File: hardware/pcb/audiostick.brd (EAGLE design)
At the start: 84 x 34 mm, 61 parts, among them IC1 TPS73633MBDV, IC3 PCM5102ASW, IC5 AP22804W5, IC6 TINY13V-10SSU, J1 AVRISP6TH127, J2 AUDIO_JACK_3.5MM_PTH, J3 USB-B, SW1 EVQP7, T1 BC850

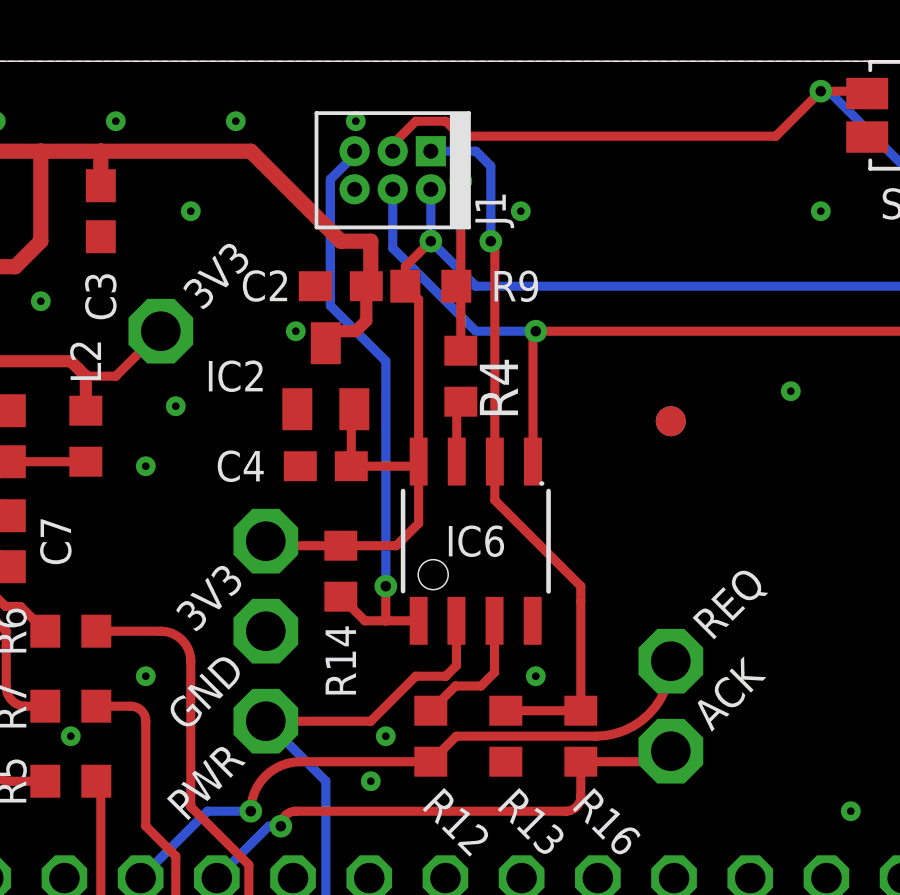
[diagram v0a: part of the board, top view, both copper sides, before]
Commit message: Update board, BOM, and firmware
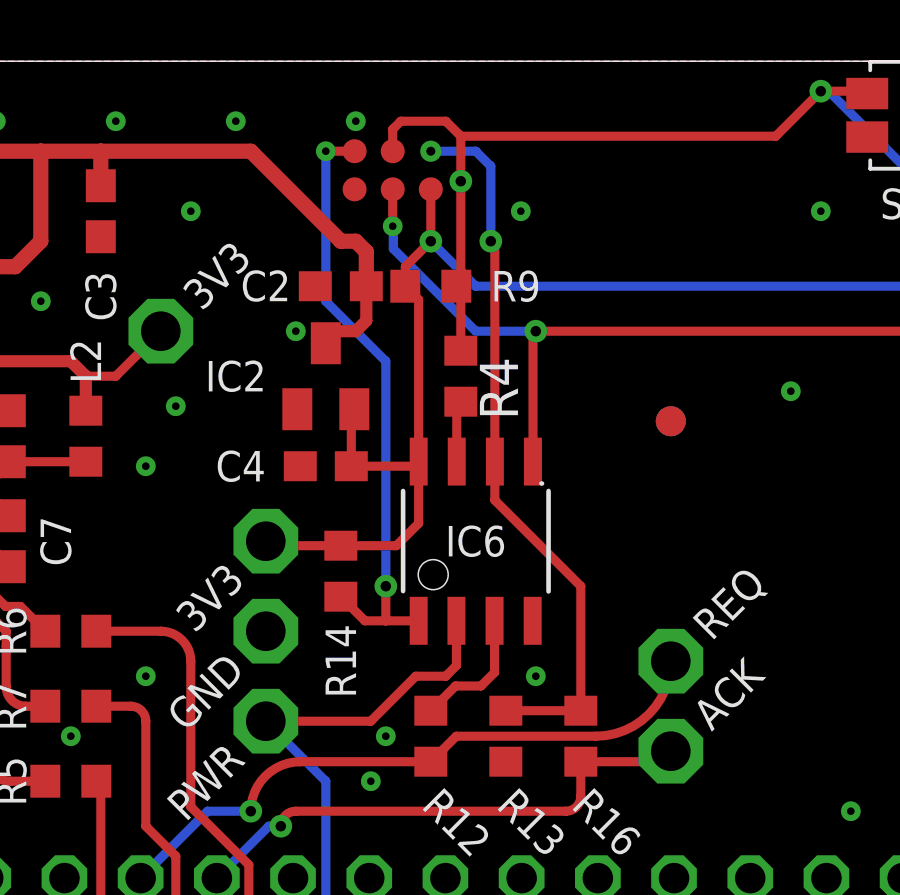
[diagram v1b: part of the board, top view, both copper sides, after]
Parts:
- removed J1: AVRISP6TH127, AWJLEagleLib:2X3-50MIL
- added TP10, TP12, TP13, TP14, TP7: PTR1TP08R, testpad:TP08R
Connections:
- net !RST: now also TP10.TP; no longer J1.5
- net +3V3: now also TP14.TP; no longer J1.2
- net ACK: no longer J1.1
- net GND: now also TP12.TP; no longer J1.6
- net LED: now also TP13.TP; no longer J1.4
- net SW: now also TP7.TP; no longer J1.3
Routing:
- net !RST: track 19.7 -> 20.4 mm, vias 1 -> 2
- net LED: vias 1 -> 2
- net ACK: vias 1 -> 2

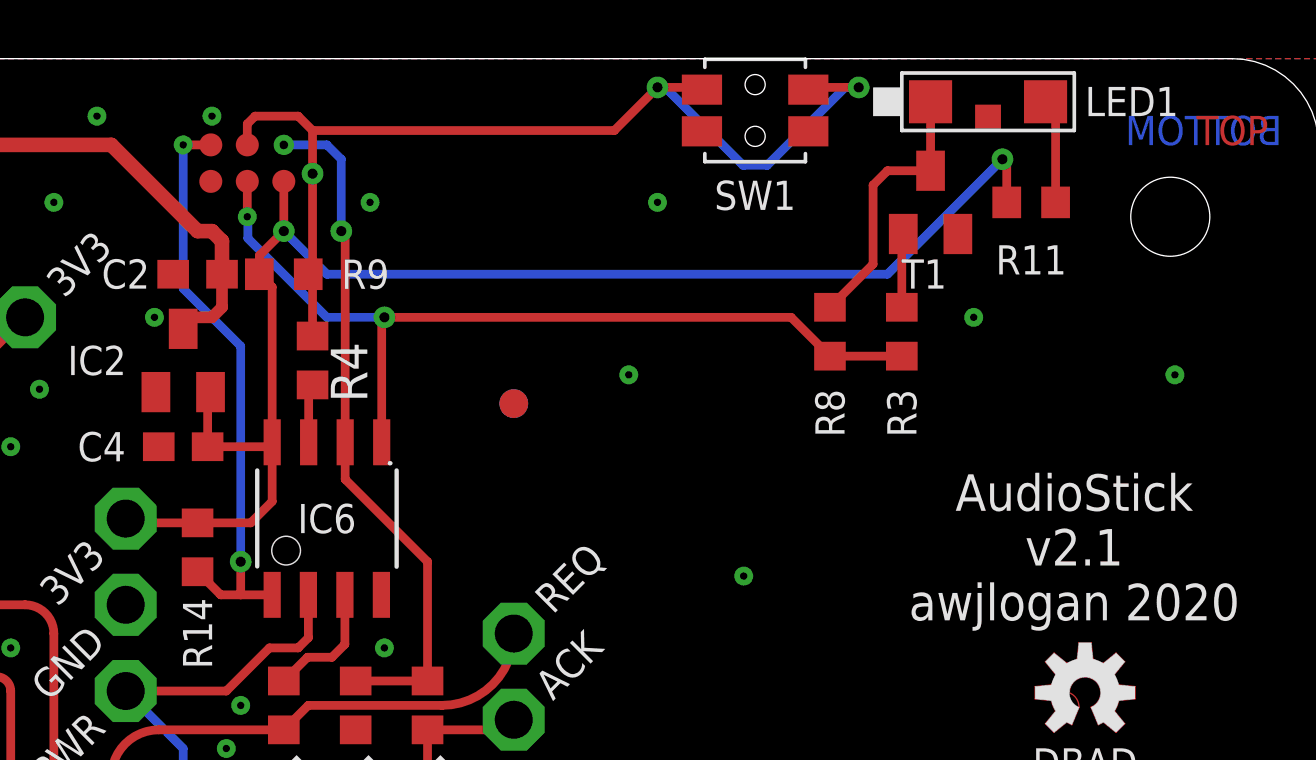
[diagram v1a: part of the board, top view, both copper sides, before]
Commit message: Changed pogo points for proper header, silly idea!
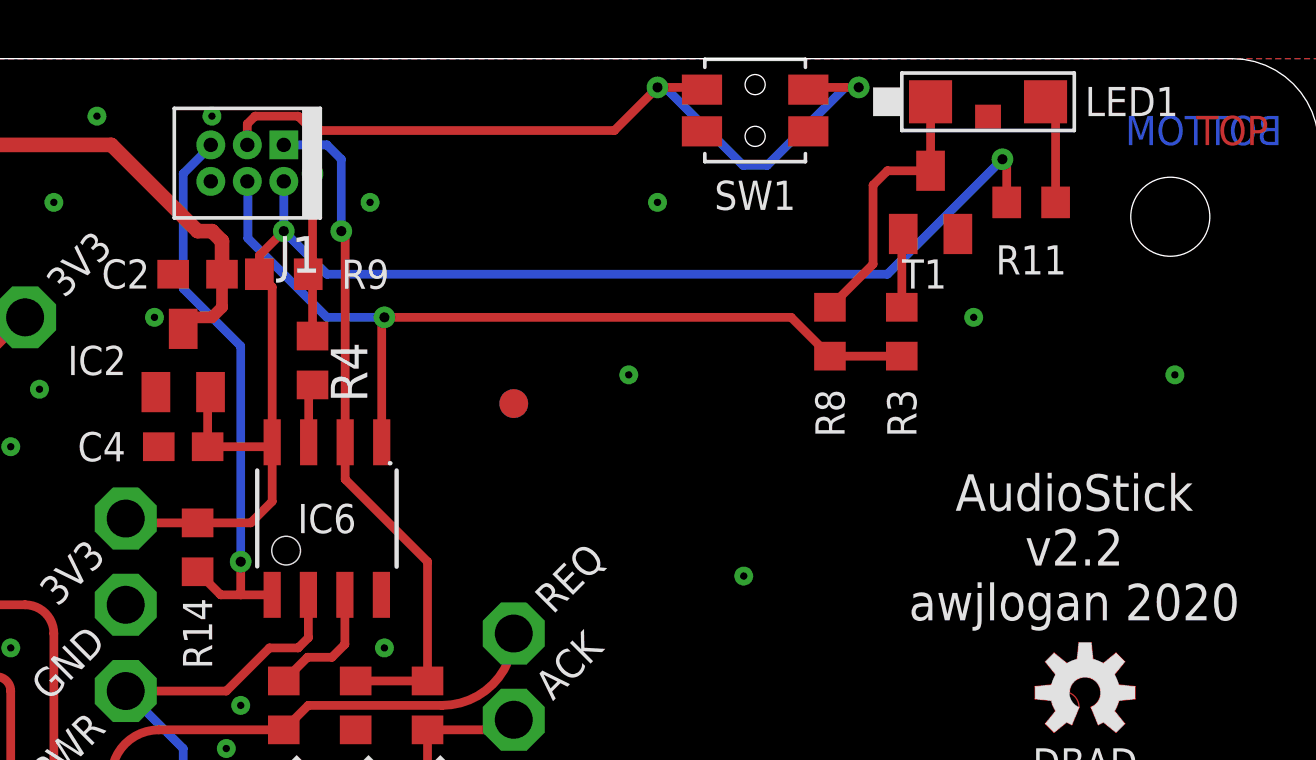
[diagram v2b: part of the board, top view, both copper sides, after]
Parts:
- removed TP10, TP12, TP13, TP14, TP7: PTR1TP08R, testpad:TP08R
- added J1: AVRISP6TH127, AWJLEagleLib:2X3-50MIL
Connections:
- net !RST: now also J1.5; no longer TP10.TP
- net +3V3: now also J1.2; no longer TP14.TP
- net ACK: now also J1.1
- net GND: now also J1.6; no longer TP12.TP
- net LED: now also J1.4; no longer TP13.TP
- net SW: now also J1.3; no longer TP7.TP
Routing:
- net !RST: track 20.4 -> 19.8 mm, vias 2 -> 1
- net LED: vias 2 -> 1
- net ACK: vias 2 -> 1
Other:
- board text added: "AudioStick v2.2 awjlogan 2020"
- board text removed: "AudioStick v2.1 awjlogan 2020"
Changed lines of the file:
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@@
 <wire x1="16" y1="3" x2="15" y2="4" width="0" layer="20" curve="90"/>
 <text x="75.5" y="17" size="1.27" layer="25" font="vector" ratio="15" rot="R180" align="center">AudioStick
-v2.1
+v2.2
 awjlogan 2020</text>
 <polygon width="0.01" layer="21">
@@
 <attribute name="NAME" x="64.397" y="28.737" size="1.016" layer="21" font="vector" ratio="21" align="bottom-center"/>
 </element>
-<element name="TP7" library="testpad" library_urn="urn:adsk.eagle:library:385" package="TP08R" package3d_urn="urn:adsk.eagle:package:27956/1" value="PTR1TP08R" x="46.73" y="31" smashed="yes">
-<attribute name="POPULARITY" value="0" x="46.73" y="31" size="1.778" layer="27" display="off"/>
-<attribute name="TP_SIGNAL_NAME" value="" x="46.73" y="31" size="1.778" layer="27" display="off"/>
-<attribute name="VALUE" x="46.476" y="30.619" size="0.0254" layer="27"/>
-</element>
-<element name="TP10" library="testpad" library_urn="urn:adsk.eagle:library:385" package="TP08R" package3d_urn="urn:adsk.eagle:package:27956/1" value="PTR1TP08R" x="45.46" y="31" smashed="yes">
-<attribute name="POPULARITY" value="0" x="45.46" y="31" size="1.778" layer="27" display="off"/>
-<attribute name="TP_SIGNAL_NAME" value="" x="45.46" y="31" size="1.778" layer="27" display="off"/>
-<attribute name="VALUE" x="45.079" y="30.619" size="0.0254" layer="27"/>
-</element>
-<element name="TP12" library="testpad" library_urn="urn:adsk.eagle:library:385" package="TP08R" package3d_urn="urn:adsk.eagle:package:27956/1" value="PTR1TP08R" x="45.46" y="29.73" smashed="yes" rot="R90">
-<attribute name="POPULARITY" value="0" x="45.46" y="29.73" size="1.778" layer="27" rot="R90" display="off"/>
-<attribute name="TP_SIGNAL_NAME" value="" x="45.46" y="29.73" size="1.778" layer="27" rot="R90" display="off"/>
-<attribute name="VALUE" x="45.841" y="29.349" size="0.0254" layer="27" rot="R90"/>
-</element>
-<element name="TP13" library="testpad" library_urn="urn:adsk.eagle:library:385" package="TP08R" package3d_urn="urn:adsk.eagle:package:27956/1" value="PTR1TP08R" x="46.73" y="29.73" smashed="yes" rot="R90">
-<attribute name="POPULARITY" value="0" x="46.73" y="29.73" size="1.778" layer="27" rot="R90" display="off"/>
-<attribute name="TP_SIGNAL_NAME" value="" x="46.73" y="29.73" size="1.778" layer="27" rot="R90" display="off"/>
-<attribute name="VALUE" x="47.111" y="29.349" size="0.0254" layer="27" rot="R90"/>
-</element>
-<element name="TP14" library="testpad" library_urn="urn:adsk.eagle:library:385" package="TP08R" package3d_urn="urn:adsk.eagle:package:27956/1" value="PTR1TP08R" x="48" y="29.73" smashed="yes" rot="R90">
-<attribute name="POPULARITY" value="0" x="48" y="29.73" size="1.778" layer="27" rot="R90" display="off"/>
-<attribute name="TP_SIGNAL_NAME" value="" x="48" y="29.73" size="1.778" layer="27" rot="R90" display="off"/>
-<attribute name="VALUE" x="48.381" y="29.349" size="0.0254" layer="27" rot="R90"/>
+<element name="J1" library="AWJLEagleLib" package="2X3-50MIL" value="AVRISP6TH127" x="48" y="31" smashed="yes" rot="R180">
+<attribute name="NAME" x="49.27" y="27.825" size="1.27" layer="25" rot="R180"/>
 </element>
 </elements>
@@
 <contactref element="SW1" pad="2A"/>
 <contactref element="SW1" pad="2B"/>
-<contactref element="TP12" pad="TP"/>
+<contactref element="J1" pad="6"/>
 </signal>
 <signal name="N$1">
@@
 <wire x1="49.5" y1="26.5" x2="69" y2="26.5" width="0.3048" layer="16"/>
 <wire x1="69" y1="26.5" x2="73" y2="30.5" width="0.3048" layer="16"/>
-<contactref element="TP14" pad="TP"/>
-<wire x1="48" y1="29.73" x2="48" y2="28" width="0.3048" layer="1"/>
+<contactref element="J1" pad="2"/>
+<wire x1="48" y1="28" x2="48" y2="29.73" width="0.3048" layer="16"/>
 </signal>
 <signal name="!RST">
@@
 <wire x1="46.5" y1="16.5" x2="46.5" y2="24" width="0.3048" layer="16"/>
 <wire x1="46.5" y1="24" x2="44.5" y2="26" width="0.3048" layer="16"/>
-<contactref element="TP10" pad="TP"/>
-<via x="44.5" y="31" extent="1-16" drill="0.254"/>
-<wire x1="45.46" y1="31" x2="44.5" y2="31" width="0.3048" layer="1"/>
-<wire x1="44.5" y1="26" x2="44.5" y2="31" width="0.3048" layer="16"/>
+<contactref element="J1" pad="5"/>
+<wire x1="44.5" y1="26" x2="44.5" y2="30" width="0.3048" layer="16"/>
+<wire x1="45.46" y1="30.96" x2="45.46" y2="31" width="0.3048" layer="16"/>
+<wire x1="44.5" y1="30" x2="45.46" y2="30.96" width="0.3048" layer="16"/>
 </signal>
 <signal name="PWR">
@@
 <signal name="SW">
 <contactref element="R9" pad="1"/>
-<wire x1="48.925" y1="26.575" x2="49" y2="26.65" width="0.3048" layer="1"/>
 <via x="49" y="30" extent="1-16" drill="0.35"/>
 <wire x1="49" y1="30" x2="49" y2="31.5" width="0.3048" layer="1"/>
@@
 <contactref element="R4" pad="1"/>
 <wire x1="49" y1="26.65" x2="49" y2="30" width="0.3048" layer="1"/>
-<wire x1="48.85" y1="26.5" x2="48.925" y2="26.575" width="0.3048" layer="1"/>
+<wire x1="48.85" y1="26.5" x2="49" y2="26.65" width="0.3048" layer="1"/>
 <wire x1="48.85" y1="26.5" x2="49" y2="26.35" width="0.3048" layer="1"/>
 <wire x1="49" y1="26.35" x2="49" y2="24.35" width="0.3048" layer="1"/>
@@
 <wire x1="61.265075" y1="33" x2="63.978475" y2="30.2866" width="0.3048" layer="16"/>
 <wire x1="64.815525" y1="30.2866" x2="67.528925" y2="33" width="0.3048" layer="16"/>
-<contactref element="TP7" pad="TP"/>
-<wire x1="46.73" y1="31" x2="46.73" y2="31.73" width="0.3048" layer="1"/>
-<wire x1="46.73" y1="31.73" x2="47" y2="32" width="0.3048" layer="1"/>
+<wire x1="47" y1="32" x2="46.73" y2="31.73" width="0.3048" layer="1"/>
 <wire x1="47" y1="32" x2="48.5" y2="32" width="0.3048" layer="1"/>
+<contactref element="J1" pad="3"/>
+<wire x1="46.73" y1="31.73" x2="46.73" y2="31" width="0.3048" layer="1"/>
 </signal>
 <signal name="S_REQ'">
@@
 <wire x1="50.135" y1="19.365" x2="53" y2="16.5" width="0.3048" layer="1"/>
 <wire x1="53" y1="12.35" x2="50.5" y2="12.35" width="0.3048" layer="1"/>
-<via x="48" y="31" extent="1-16" drill="0.3" diameter="0.7" shape="square"/>
 <wire x1="49.5" y1="31" x2="48" y2="31" width="0.3048" layer="16"/>
+<contactref element="J1" pad="1"/>
 </signal>
 <signal name="REQ">
@@
 <wire x1="51.405" y1="20.654" x2="51.405" y2="25.095" width="0.3048" layer="1"/>
 <wire x1="49.5" y1="25" x2="51.5" y2="25" width="0.3048" layer="16"/>
-<wire x1="46.75" y1="27.75" x2="49.5" y2="25" width="0.3048" layer="16"/>
+<wire x1="49.5" y1="25" x2="46.75" y2="27.75" width="0.3048" layer="16"/>
 <wire x1="69.5" y1="23.65" x2="67" y2="23.65" width="0.3048" layer="1"/>
 <wire x1="51.5" y1="25" x2="65.65" y2="25" width="0.3048" layer="1"/>
 <wire x1="65.65" y1="25" x2="67" y2="23.65" width="0.3048" layer="1"/>
-<contactref element="TP13" pad="TP"/>
-<via x="46.73" y="28.5" extent="1-16" drill="0.254"/>
-<wire x1="46.73" y1="28.5" x2="46.73" y2="29.73" width="0.3048" layer="1"/>
-<wire x1="46.73" y1="28.5" x2="46.75" y2="28.48" width="0.3048" layer="16"/>
-<wire x1="46.75" y1="28.48" x2="46.75" y2="27.75" width="0.3048" layer="16"/>
+<contactref element="J1" pad="4"/>
+<wire x1="46.75" y1="29.71" x2="46.73" y2="29.73" width="0.3048" layer="16"/>
+<wire x1="46.75" y1="27.75" x2="46.75" y2="29.71" width="0.3048" layer="16"/>
 </signal>
 <signal name="N$18">

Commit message: Finish schematic/layout changes
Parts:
- removed J1: AVRISP6TH127, AWJLEagleLib:2X3-50MIL
- added J4: AVRISP, AudioStick:2X3-1.27
- C14, C3: value 4u7 -> 2u2
- IC1: value TPS73633MBDV -> AP2127K
- R10: value 100K -> 10K
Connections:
- net !RST: now also J4.3; no longer J1.5
- net +3V3: now also J4.6; no longer J1.2
- net ACK: now also J4.1; no longer J1.1
- net GND: now also J4.4; no longer J1.6
- net LED: now also J4.5; no longer J1.4
- net SW: now also J4.2; no longer J1.3
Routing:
- net SW: track 35.8 -> 35.3 mm, vias 3 -> 2
